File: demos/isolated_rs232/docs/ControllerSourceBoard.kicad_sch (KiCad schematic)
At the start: 1 part, among them P1 Header1xNMale

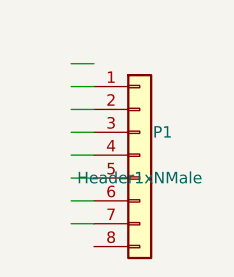
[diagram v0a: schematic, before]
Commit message: export: kicad_sch — Phase 2.5b: layered placement, wire routing, KiCad 10 compatibility (#23)
* export: kicad_sch — Phase 2.5b: layered placement + routing + KiCad 9 fix

Placement (placement.py, complete rewrite):
- Replaces naive grid with Layered Signal Flow algorithm (spec §5 stages 1–8)
- Stage 1: band classification — power chips/rails at top, LEDs at bottom,
  everything else in the signal band
- Stage 2: signal-flow DAG via BFS from Rail/Connector sources; layer = BFS
  distance from nearest source
- Stage 3–4: place within (band, layer) cells at 1500-mil (38.1 mm) same-band
  spacing, 1000-mil inter-band gutter, 25.4 mm page margin
- Stage 6: cluster breakup — up to 10 iterations shifting same-band parts
  that land closer than 0.9× SAME_BAND_SPACING_MM
- Stage 8: page sized to fit (A4 → A3 → A2 → A1)
- grid_place() and sheet_size_mm() kept as shims for backward-compat

Routing (routing.py, new file):
- route_net(): connects stub ends with Manhattan L-shapes (horizontal first)
- find_junctions(): returns points where ≥3 wire endpoints coincide
- renderer uses routed wires between signal-net stub ends

Hierarchical (hierarchical.py, new file):
- collect_boards(), is_multi_board(), sub_sheet_filename() — interface stub
  for multi-Board sub-sheet emission (full implementation deferred)

KiCad 9 sub-symbol name fix (library_loader.py):
- KiCad 9 schematics expect sub-symbols nested inside their parent in
  lib_symbols to use the bare name (R_0_1, LED_0_1, 4069_1_0) — NOT the
  lib-qualified name (Device:R_0_1, Device:LED_0_1, 4xxx:4069_1_0)
- Fixed _qualify_names() to add the lib: prefix only to the exact parent
  symbol name using a lookahead (?=") that prevents sub-unit names from
  being qualified

Tests (+25 tests):
- test_placement.py: band classification, all-on-grid, determinism,
  minimum spacing, power < signal < indicator Y ordering, page sizing
- test_routing.py: H/V segments, L-shapes, orthogonality, grid snap,
  junction detection

Golden files re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
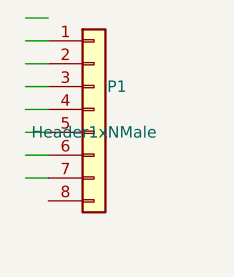
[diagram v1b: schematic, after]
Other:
- moved on the sheet: P1
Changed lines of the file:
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@@
 (kicad_sch
-  (version 20240618)
+  (version 20250114)
   (generator "wirebench")
-  (generator_version "0.1")
+  (generator_version "0.2")
   (paper "A4")
   (symbol
     (lib_id "Connector_Generic:Conn_01x08")
-    (at 30.48 30.48 0)
+    (at 25.4 25.4 0)
     (unit 1)
     (exclude_from_sim no)
@@
     (dnp no)
     (property "Reference" "P1"
-      (at 33.02 27.94 0)
+      (at 27.94 22.86 0)
       (effects (font (size 1.27 1.27)))
     )
     (property "Value" "Header1xNMale"
-      (at 30.48 33.02 0)
+      (at 25.4 27.94 0)
       (effects (font (size 1.27 1.27)))
     )
@@
   )
   (wire
-    (pts (xy 25.4 38.1) (xy 22.86 38.1))
+    (pts (xy 20.32 33.02) (xy 17.78 33.02))
     (stroke (width 0) (type default))
   )
   (wire
-    (pts (xy 25.4 35.56) (xy 22.86 35.56))
+    (pts (xy 20.32 30.48) (xy 17.78 30.48))
     (stroke (width 0) (type default))
   )
   (wire
-    (pts (xy 25.4 33.02) (xy 22.86 33.02))
+    (pts (xy 20.32 27.94) (xy 17.78 27.94))
     (stroke (width 0) (type default))
   )
   (wire
-    (pts (xy 25.4 30.48) (xy 22.86 30.48))
+    (pts (xy 20.32 25.4) (xy 17.78 25.4))
     (stroke (width 0) (type default))
   )
   (wire
-    (pts (xy 25.4 27.94) (xy 22.86 27.94))
+    (pts (xy 20.32 22.86) (xy 17.78 22.86))
     (stroke (width 0) (type default))
   )
   (wire
-    (pts (xy 25.4 25.4) (xy 22.86 25.4))
+    (pts (xy 20.32 20.32) (xy 17.78 20.32))
     (stroke (width 0) (type default))
   )
   (wire
-    (pts (xy 25.4 22.86) (xy 22.86 22.86))
+    (pts (xy 20.32 17.78) (xy 17.78 17.78))
     (stroke (width 0) (type default))
   )
   (wire
-    (pts (xy 25.4 20.32) (xy 22.86 20.32))
+    (pts (xy 20.32 15.24) (xy 17.78 15.24))
     (stroke (width 0) (type default))
   )
